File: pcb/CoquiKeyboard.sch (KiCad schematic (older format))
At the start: 116 parts

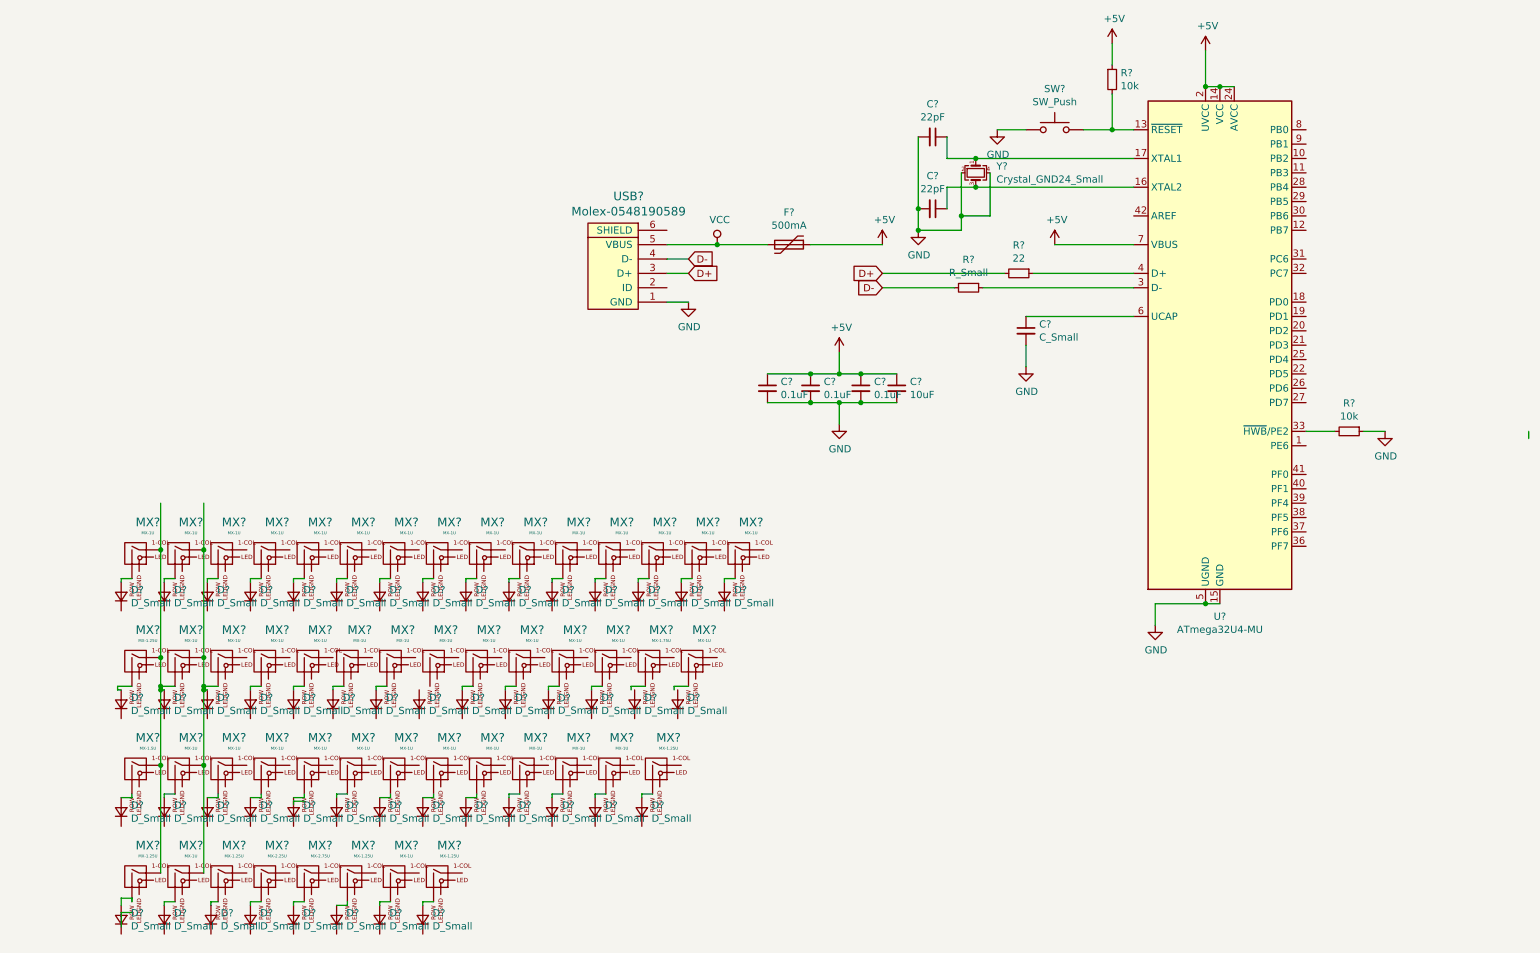
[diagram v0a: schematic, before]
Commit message: label components
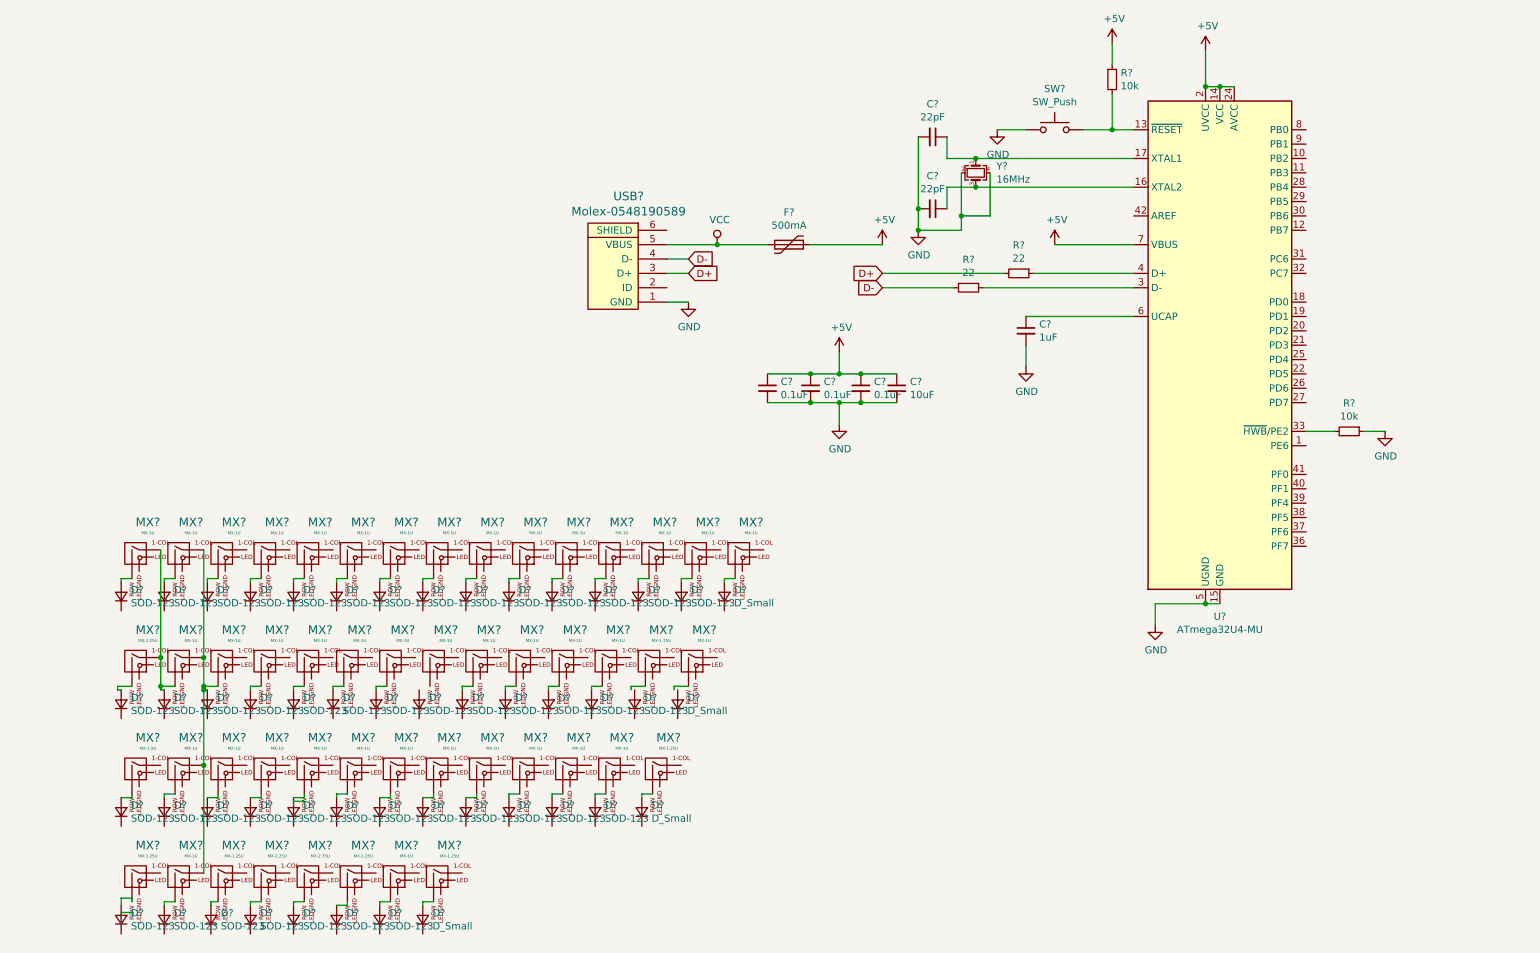
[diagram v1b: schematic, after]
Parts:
- C?: value C_Small -> 1uF
- D? (x46): value D_Small -> SOD-123
- R?: value R_Small -> 22
- Y?: value Crystal_GND24_Small -> 16MHz
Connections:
- wire segments 166 -> 161

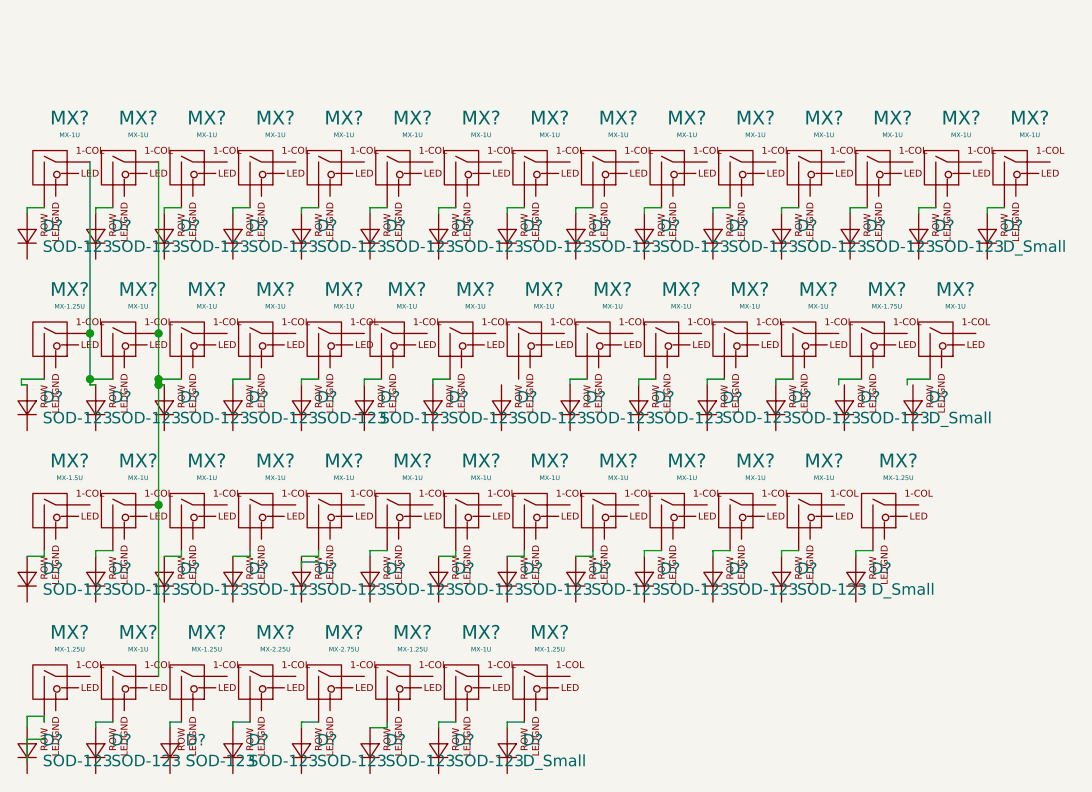
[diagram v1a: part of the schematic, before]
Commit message: connect diodes to switches
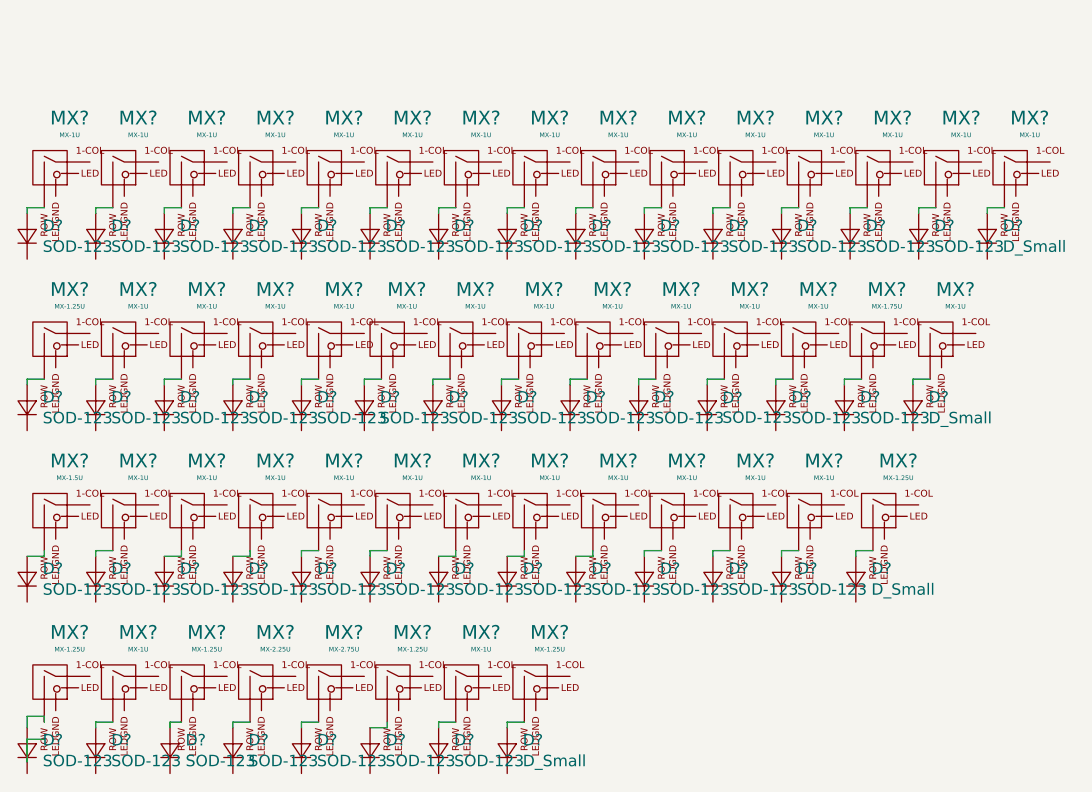
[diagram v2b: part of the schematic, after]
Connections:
- wire segments 161 -> 152
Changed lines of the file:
@@
 	5400 4525 5475 4525
 Wire Wire Line
-	1475 5275 1575 5275
-Wire Wire Line
 	4500 4550 4500 4525
 Wire Wire Line
 	4500 4525 4575 4525
-Wire Wire Line
-	1775 5275 1875 5275
-Wire Wire Line
-	1175 5275 1275 5275
-Wire Wire Line
-	4750 5300 4750 5275
-Wire Wire Line
-	4750 5275 4850 5275
-Wire Wire Line
-	5050 5300 5050 5275
-Wire Wire Line
-	5050 5275 5150 5275
-Wire Wire Line
-	2400 6100 2400 6075
-Wire Wire Line
-	2400 6075 2475 6075
 $Comp
 L Device:D_Small D?
@@
 	1200 6850 1275 6850
 Wire Wire Line
-	1175 5275 1175 5300
-Wire Wire Line
 	4825 6050 4825 6025
 Wire Wire Line
@@
 	2700 6800 2775 6800
 Wire Wire Line
-	1175 5300 1200 5300
-Wire Wire Line
-	1475 5300 1500 5300
-Wire Wire Line
-	1775 5300 1800 5300
-Wire Wire Line
 	1200 6050 1275 6050
 Wire Wire Line
@@
 	2175 6050 2175 6025
 Wire Wire Line
-	2400 6050 2475 6050
-Wire Wire Line
-	2475 6050 2475 6025
-Wire Wire Line
 	2700 6050 2700 6025
 Wire Wire Line
@@
 	3300 6775 3375 6775
 Wire Wire Line
-	1475 4325 1475 5075
-Connection ~ 1475 5075
-Wire Wire Line
-	1475 5075 1475 5275
-Connection ~ 1475 5275
-Wire Wire Line
-	1475 5275 1475 5300
-Wire Wire Line
-	1775 4325 1775 5075
-Connection ~ 1775 5075
-Wire Wire Line
-	1775 5075 1775 5275
-Connection ~ 1775 5275
-Wire Wire Line
-	1775 5275 1775 5300
-Connection ~ 1775 5300
-Wire Wire Line
-	1775 5300 1775 5825
-Connection ~ 1775 5825
-Wire Wire Line
-	1775 5825 1775 6575
-Wire Wire Line
 	2100 5300 2100 5275
 Wire Wire Line
@@
 Wire Wire Line
 	4175 5275 4175 5300
+Wire Wire Line
+	3275 5300 3275 5275
+Wire Wire Line
+	3275 5275 3350 5275
+Wire Wire Line
+	4775 5300 4775 5275
+Wire Wire Line
+	4775 5275 4850 5275
+Wire Wire Line
+	5075 5300 5075 5275
+Wire Wire Line
+	5075 5275 5150 5275
+Wire Wire Line
+	1200 5300 1200 5275
+Wire Wire Line
+	1200 5275 1275 5275
+Wire Wire Line
+	1500 5300 1500 5275
+Wire Wire Line
+	1500 5275 1575 5275
+Wire Wire Line
+	1800 5300 1800 5275
+Wire Wire Line
+	1800 5275 1875 5275
+Wire Wire Line
+	2400 6050 2400 6025
+Wire Wire Line
+	2400 6025 2475 6025
 $EndSCHEMATC
